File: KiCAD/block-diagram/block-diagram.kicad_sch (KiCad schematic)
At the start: 16 parts, among them Q3 NMOS, Q4 NMOS, SW1 SW_Push, SW2 SW, SW3 SW, SW4 SW_SPST, U1 74LS02, U2 74LS02, U3 74LS11, U6 LMC555xM

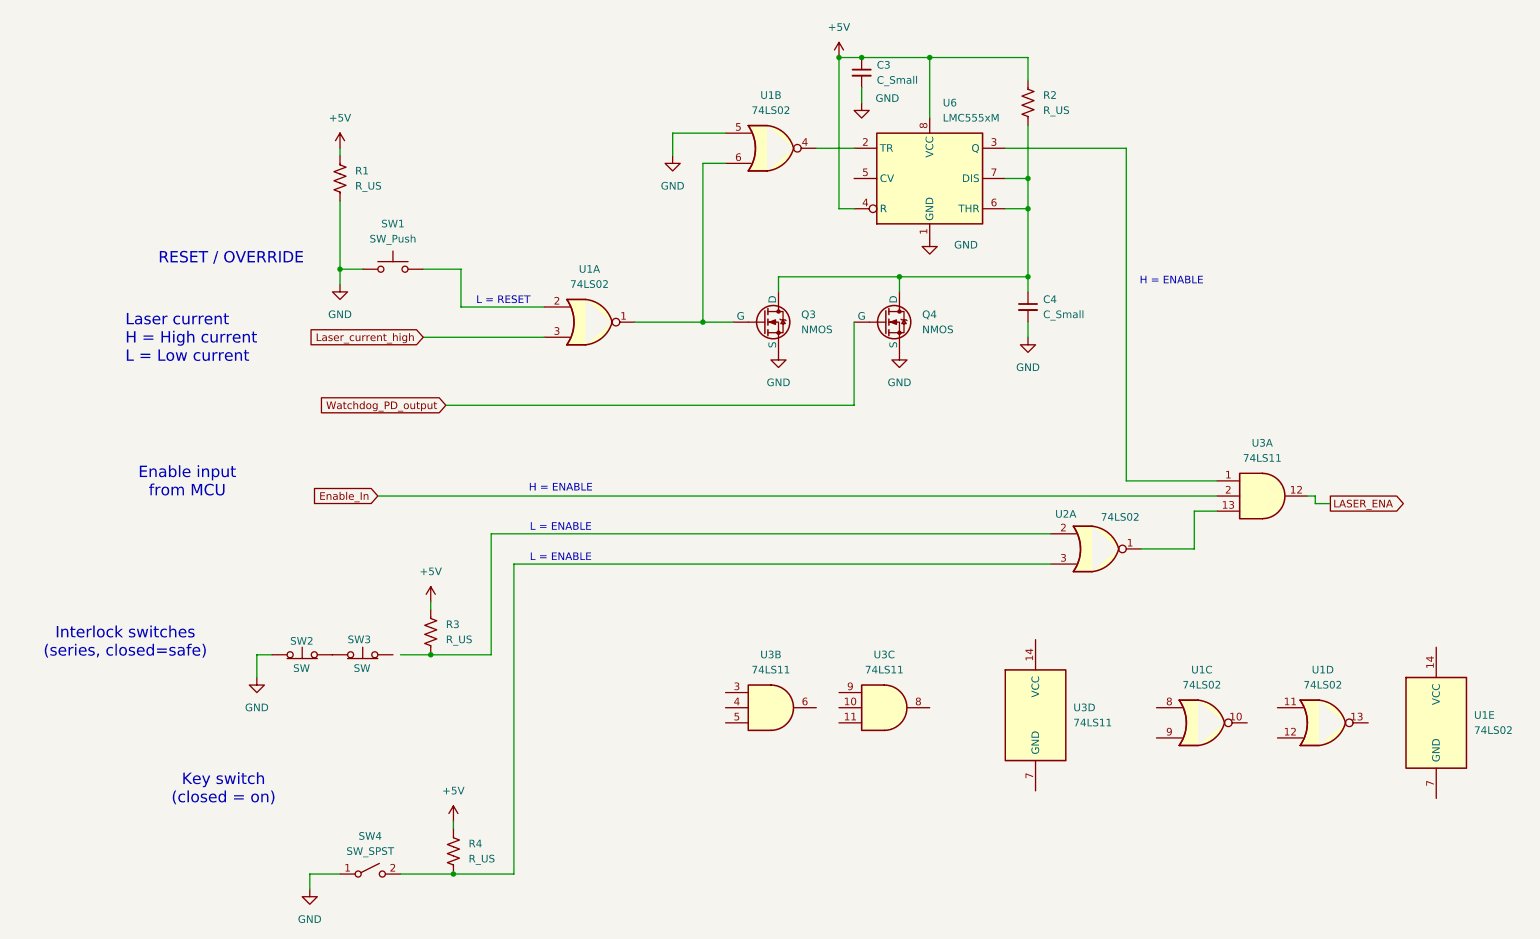
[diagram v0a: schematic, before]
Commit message: Add board-to-board connectors
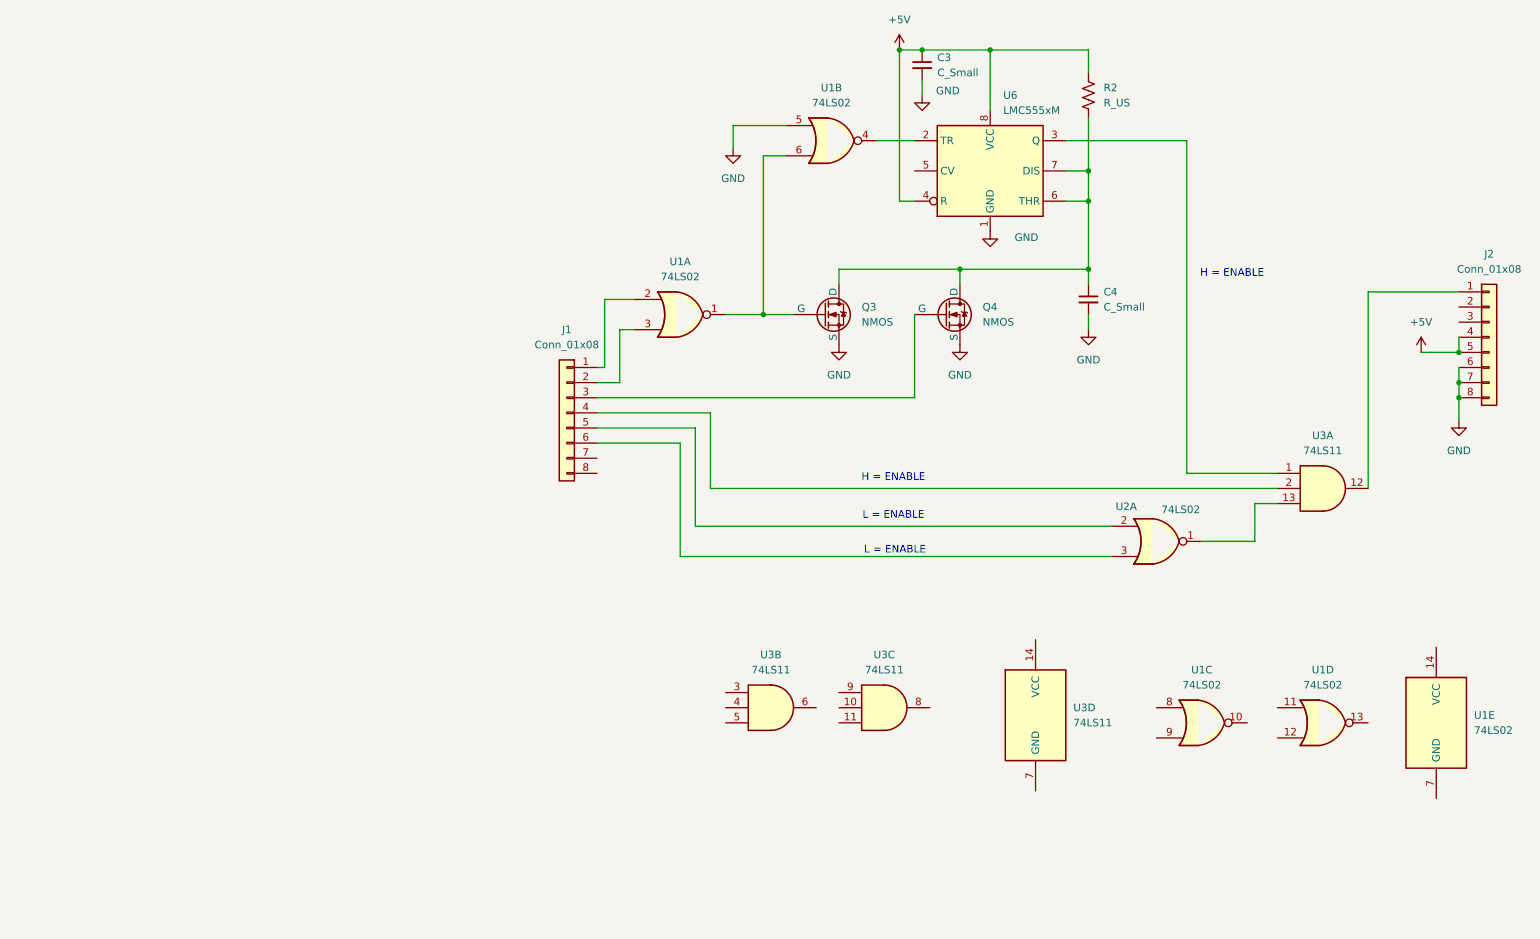
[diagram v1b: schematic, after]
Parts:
- removed R1, R3, R4: R_US, symbol Device:R_US
- removed SW1: SW_Push, symbol Switch:SW_Push
- removed SW2, SW3: SW, symbol Switch:SW_Push_Open
- removed SW4: SW_SPST, symbol Switch:SW_SPST
- added J1, J2: Conn_01x08, symbol Connector_Generic:Conn_01x08
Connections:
- net +5V: now also J2.4 (Pin_4), J2.5 (Pin_5)
- net GND: now also J2.6 (Pin_6), J2.7 (Pin_7), J2.8 (Pin_8)
- net at U2.2: now also J1.5 (Pin_5)
- net at U2.3: now also J1.6 (Pin_6)
- net at U1.2: now also J1.1 (Pin_1)
- net Enable_In: no longer names the net of U3.2
- net Enable_In: now also J1.4 (Pin_4)
- net LASER_ENA: no longer names the net of U3.12
- net LASER_ENA: now also J2.1 (Pin_1)
- net Laser_current_high: no longer names the net of U1.3
- net Laser_current_high: now also J1.2 (Pin_2)
- net Watchdog_PD_output: no longer names the net of Q4.2 (G)
- net Watchdog_PD_output: now also J1.3 (Pin_3)
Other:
- note removed: "Enable input from MCU"
- note removed: "Interlock switches (series, closed=safe)"
- note removed: "Key switch (closed = on)"
- note removed: "L = RESET"
- note removed: "Laser current H = High current L = Low current"
- note removed: "RESET / OVERRIDE"
- moved on the sheet: C3, C4, Q3, Q4, R2, U1A, U1B, U2A, U3A, U6
